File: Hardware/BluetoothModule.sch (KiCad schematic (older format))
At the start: 9 parts, among them J4 Conn_01x06_Male, SW2 SW_DIP_x01, SW3 SW_Push, U9 HC-05

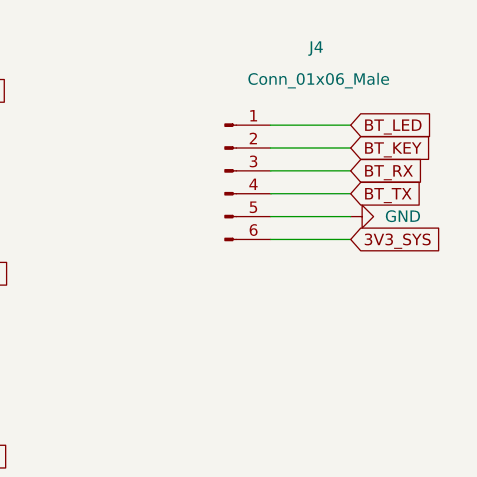
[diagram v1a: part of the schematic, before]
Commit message: Changed HC-05 pins for other Forbot HC-05
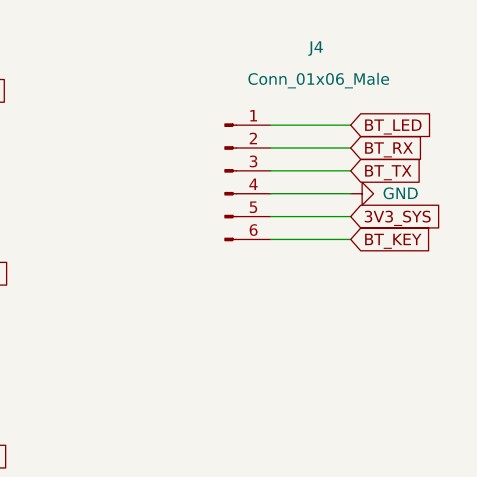
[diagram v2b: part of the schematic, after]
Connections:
- net 3V3_SYS: now also J4.5 (Pin_5); no longer J4.6 (Pin_6)
- net BT_KEY: now also J4.6 (Pin_6); no longer J4.2 (Pin_2)
- net BT_RX: now also J4.2 (Pin_2); no longer J4.3 (Pin_3)
- net BT_TX: now also J4.3 (Pin_3); no longer J4.4 (Pin_4)
- net GND: now also J4.4 (Pin_4); no longer J4.5 (Pin_5)
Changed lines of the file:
@@
 $EndComp
 Connection ~ 3730 4120
+Text GLabel 6630 3070 2    50   Input ~ 0
+BT_RX
 Text GLabel 6630 3170 2    50   Input ~ 0
-BT_RX
-Text GLabel 6630 3270 2    50   Input ~ 0
 BT_TX
-Text GLabel 6630 3070 2    50   Input ~ 0
+Text GLabel 6630 3470 2    50   Input ~ 0
 BT_KEY
 $Comp
@@
 L power:GND #PWR034
 U 1 1 606BEA53
-P 6630 3370
-F 0 "#PWR034" H 6630 3120 50  0001 C CNN
-F 1 "GND" V 6630 3220 50  0000 R CNN
-F 2 "" H 6630 3370 50  0001 C CNN
-F 3 "" H 6630 3370 50  0001 C CNN
-	1    6630 3370
+P 6630 3270
+F 0 "#PWR034" H 6630 3020 50  0001 C CNN
+F 1 "GND" V 6630 3130 50  0000 R CNN
+F 2 "" H 6630 3270 50  0001 C CNN
+F 3 "" H 6630 3270 50  0001 C CNN
+	1    6630 3270
 	0    -1   -1   0
 $EndComp
@@
 Text GLabel 4780 4720 2    50   Input ~ 0
 3V3_SYS
-Text GLabel 6630 3470 2    50   Input ~ 0
+Text GLabel 6630 3370 2    50   Input ~ 0
 3V3_SYS
 $Comp
